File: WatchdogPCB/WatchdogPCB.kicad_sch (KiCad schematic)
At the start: 5 parts, among them J1 Conn_01x05_Socket, J2 Conn_01x05_Pin, J3 Screw_Terminal_01x03, J4 Power

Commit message: Working on the schematic
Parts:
- removed J1: Conn_01x05_Socket, Connector_Molex:Molex_KK-254_AE-6410-05A_1x05_P2.54mm_Vertical, symbol Connector:Conn_01x05_Socket
- removed J2: Conn_01x05_Pin, Connector_PinHeader_2.54mm:PinHeader_1x05_P2.54mm_Vertical, symbol Connector:Conn_01x05_Pin
- removed J3: Screw_Terminal_01x03, TerminalBlock:TerminalBlock_bornier-3_P5.08mm, symbol Connector:Screw_Terminal_01x03
- removed J4: Power, TerminalBlock:TerminalBlock_bornier-4_P5.08mm, symbol Connector:Screw_Terminal_01x04
- added J1: Screw_Terminal_01x03, symbol Connector:Screw_Terminal_01x03
- added J2: Screw_Terminal_01x04, symbol Connector:Screw_Terminal_01x04
- added J3: Screw_Terminal_01x02, symbol Connector:Screw_Terminal_01x02
- added J4: Conn_01x05_Pin, symbol Connector:Conn_01x05_Pin
- added JP1: Jumper_2_Open, symbol Jumper:Jumper_2_Open
- added JP2: Jumper_2_Bridged, symbol Jumper:Jumper_2_Bridged
- added R1, R2, R3, R4, R5, R6: R, symbol Device:R
- added RV1: R_Potentiometer, symbol Device:R_Potentiometer
- added TH1: Thermistor_NTC, symbol Device:Thermistor_NTC
- added U1: MCP602, symbol Amplifier_Operational:MCP602
- added U2: A1301EUA-T, symbol Sensor_Magnetic:A1301EUA-T
- added U3: DS3695N, DIP254P762X508-8, symbol DS3695N:DS3695N
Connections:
- net at A1.1 (D1/TX): now also U3.4 (DI)
- net at A1.10 (D7): now also U3.3 (DE)
- net at A1.19 (A0): now also R4.1
- net at A1.2 (D0/RX): now also U3.1 (RO)
- net at A1.20 (A1): now also R5.2, R6.1
- net +5V: now reaches A1.27 (+5V)
- net +5V: now also JP2.2 (B), RV1.1, U1.8 (V+), U3.8 (VCC)
- net GND: now reaches A1.29 (GND)
- net GND: now also A1.4 (GND), J2.4 (Pin_4), J3.2 (Pin_2), R3.2, R6.2, RV1.3, TH1.2, U1.4 (V-), U3.5 (GND)
- net at A1.30 (VIN): now also JP1.1 (A)
- net at A1.5 (D2): now also R2.2, U1.1
- net at A1.7 (D4): now also U3.2 (~{RE})
- new net: J3.1 (Pin_1), R3.1, R4.2, TH1.1
- new net: J4.1 (Pin_1), JP2.1 (A)
- new net: U1.5 (+), U1.6 (-)
- new net: R1.1, R2.1, U1.3 (+)
- new net: J1.2 (Pin_2), R1.2, U2.3 (VOUT)
- new net: RV1.2, U1.2 (-)
- new net: J1.3 (Pin_3), U2.1 (VCC)
- new net: J1.1 (Pin_1), U2.2 (GND)
- new net: J2.1 (Pin_1), U3.6 (DO/RI)
- new net: J2.2 (Pin_2), U3.7 (~{DO/}RI)
- new net +12V: J2.3 (Pin_3), JP1.2 (B), R5.1
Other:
- company: (none) -> Jotham Gates
- title: (none) -> Tractor Engine Watchdog

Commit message: Schematic finished
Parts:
- removed J1: Screw_Terminal_01x03, symbol Connector:Screw_Terminal_01x03
- removed J3: Screw_Terminal_01x02, symbol Connector:Screw_Terminal_01x02
- removed R3, R4: R, symbol Device:R
- added D1: D_Zener, symbol Device:D_Zener
- added D2: 1N5404, Diode_THT:D_DO-201AD_P15.24mm_Horizontal, symbol Diode:1N5404
- added F1: 3A, symbol Device:Fuse
- added J1: Oil pressure, symbol Connector:Screw_Terminal_01x01
- added J3: Hall effect speed, symbol Connector:Screw_Terminal_01x03
- added J5: Power, symbol Connector:Screw_Terminal_01x04
- added J6, J7: Thermistor 1, symbol Connector:Screw_Terminal_01x02
- added J8: Dashboard A, symbol Connector:Conn_01x03_Pin
- added J9: Dashboard B, symbol Connector:Conn_01x05_Pin
- added R1, R7, R8: 1k, symbol Device:R
- added R10, R9: 470, symbol Device:R
- added R2: 4.7k, symbol Device:R
- added TH2: Thermistor_NTC, symbol Device:Thermistor_NTC
- J2: value Screw_Terminal_01x04 -> Roll hoop
- J4: value Conn_01x05_Pin -> H bridge driver control
- JP1: renamed from JP2; value Jumper_2_Bridged -> 5V jumper
- JP2: renamed from JP1; value Jumper_2_Open -> 12V jumper
- R3: renamed from R1; value R -> 4.7k
- R4: renamed from R2; value R -> 120k
- R5: value R -> 100k
- R6: value R -> 39k
- RV1: value R_Potentiometer -> 10k
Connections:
- net +12V: now also D2.1 (K), J5.2 (Pin_2), R10.1, R9.1; no longer R5.1
- net +5V: now also U2.1 (VCC), J3.1 (Pin_1), J9.1 (Pin_1), J9.2 (Pin_2)
- net GND: now also U1.5 (+), U2.2 (GND), D1.2 (A), J3.3 (Pin_3), J5.3 (Pin_3), J5.4 (Pin_4), J6.2 (Pin_2), J7.2 (Pin_2), J8.2 (Pin_2), J8.3 (Pin_3), J9.5 (Pin_5), R1.2, TH2.2
- net at A1.19 (A0): now also R7.1
- net at TH1.1: now also J6.1 (Pin_1), R7.2, R9.2
- net at A1.11 (D8): now also D1.1 (K), R2.2
- net at A1.14 (D11): now also J4.5 (Pin_5)
- net at R5.2, R6.1: now also A1.21 (A2); no longer A1.20 (A1)
- net Button: now reaches A1.22 (A3)
- net Button: now also J8.1 (Pin_1)
- net SDA: now reaches A1.23 (A4)
- net SDA: now also J9.3 (Pin_3)
- net SCL: now reaches A1.24 (A5)
- net SCL: now also J9.4 (Pin_4)
- net at A1.6 (D3): now also J4.2 (Pin_2)
- net at A1.8 (D5): now also J4.3 (Pin_3)
- net at A1.9 (D6): now also J4.4 (Pin_4)
- net at U1.6 (-): now also U1.7; no longer U1.5 (+)
- net at R3.2, U2.3 (VOUT): now also J3.2 (Pin_2)
- net Threshold adjust: now reaches RV1.2, U1.2 (-)
- new net: J7.1 (Pin_1), R10.2, R8.2, TH2.1
- new net: A1.20 (A1), R8.1
- new net: J1.1 (Pin_1), R1.1, R2.1
- new net +BATT: D2.2 (A), F1.1, R5.1
- new net Power in: F1.2, J5.1 (Pin_1)
- no-connect marks 0 -> 10
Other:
- note added: "Battery voltage divider"
- note added: "Dashboard"
- note added: "H bridge control pins"
- note added: "Hall effect engine speed sensor"
- note added: "NTC Thermistors"
- note added: "Oil pressure switch"
- note added: "Power input and H bridge power"
- note added: "RS485 connection to roll hoop"
- note added: "Unused op amp"
- moved on the sheet: J2, J4, JP1, R3, R4, R5, R6, RV1, U1A, U1B, U2, U3

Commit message: Layout mostly done
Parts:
- removed J1: Oil pressure, symbol Connector:Screw_Terminal_01x01
- removed J3: Hall effect speed, symbol Connector:Screw_Terminal_01x03
- added H1, H2, H3, H4: MountingHole, MountingHole:MountingHole_3.2mm_M3_Pad, symbol Mechanical:MountingHole
- added J2: Speed & Oil, TerminalBlock:TerminalBlock_bornier-4_P5.08mm, symbol Connector:Screw_Terminal_01x04
- added R11, R12: 4.7k, Resistor_THT:R_Axial_DIN0207_L6.3mm_D2.5mm_P7.62mm_Horizontal, symbol Device:R
- D1: value D_Zener -> 5.1V; footprint (none) -> Diode_THT:D_A-405_P10.16mm_Horizontal
- F1: footprint (none) -> Fuse:Fuse_Blade_ATO_directSolder
- J1: renamed from J2; footprint (none) -> TerminalBlock:TerminalBlock_bornier-4_P5.08mm
- J3: renamed from J4; footprint (none) -> Connector_PinHeader_2.54mm:PinHeader_1x05_P2.54mm_Vertical
- J4: renamed from J5; footprint (none) -> TerminalBlock:TerminalBlock_bornier-4_P5.08mm
- J5: renamed from J6; footprint (none) -> TerminalBlock:TerminalBlock_bornier-2_P5.08mm
- J6: renamed from J7; value Thermistor 1 -> Thermistor 2; footprint (none) -> TerminalBlock:TerminalBlock_bornier-2_P5.08mm
- J7: renamed from J8; footprint (none) -> Connector_JST:JST_XH_B3B-XH-A_1x03_P2.50mm_Vertical
- J8: renamed from J9; footprint (none) -> Connector_JST:JST_XH_B5B-XH-A_1x05_P2.50mm_Vertical
- JP1, JP2: footprint (none) -> Connector_PinSocket_2.54mm:PinSocket_1x02_P2.54mm_Vertical
- R1: renamed from R3; footprint (none) -> Resistor_THT:R_Axial_DIN0207_L6.3mm_D2.5mm_P7.62mm_Horizontal
- R10, R5, R6, R7, R8, R9: footprint (none) -> Resistor_THT:R_Axial_DIN0207_L6.3mm_D2.5mm_P7.62mm_Horizontal
- R2: renamed from R1; footprint (none) -> Resistor_THT:R_Axial_DIN0207_L6.3mm_D2.5mm_P7.62mm_Horizontal
- R3: renamed from R4; footprint (none) -> Resistor_THT:R_Axial_DIN0207_L6.3mm_D2.5mm_P7.62mm_Horizontal
- R4: renamed from R2; footprint (none) -> Resistor_THT:R_Axial_DIN0207_L6.3mm_D2.5mm_P7.62mm_Horizontal
- RV1: footprint (none) -> Potentiometer_THT:Potentiometer_Piher_PT-10-V10_Vertical_Hole
- U2: renamed from U1; footprint (none) -> Package_DIP:DIP-8_W7.62mm_Socket_LongPads
- U3: footprint DIP254P762X508-8 -> Package_DIP:DIP-8_W7.62mm_Socket_LongPads
- renumbered U2 to U1
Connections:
- net +12V: no longer R10.1, R9.1
- net +5V: now also R10.1, R9.1, J2.1 (Pin_1), R11.1, R12.1
- net GND: now also J2.3 (Pin_3)
- net SCL: now also R12.2
- net SDA: now also R11.2
- net Hall effect: now reaches R1.2, U1.3 (VOUT)
- net Hall effect: now also J2.2 (Pin_2)
- net Oil: now reaches R2.1, R4.1
- net Oil: now also J2.4 (Pin_4)
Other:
- moved on the sheet: D1, R1, R2, R3, R4, RV1, U1, U2A, U2B

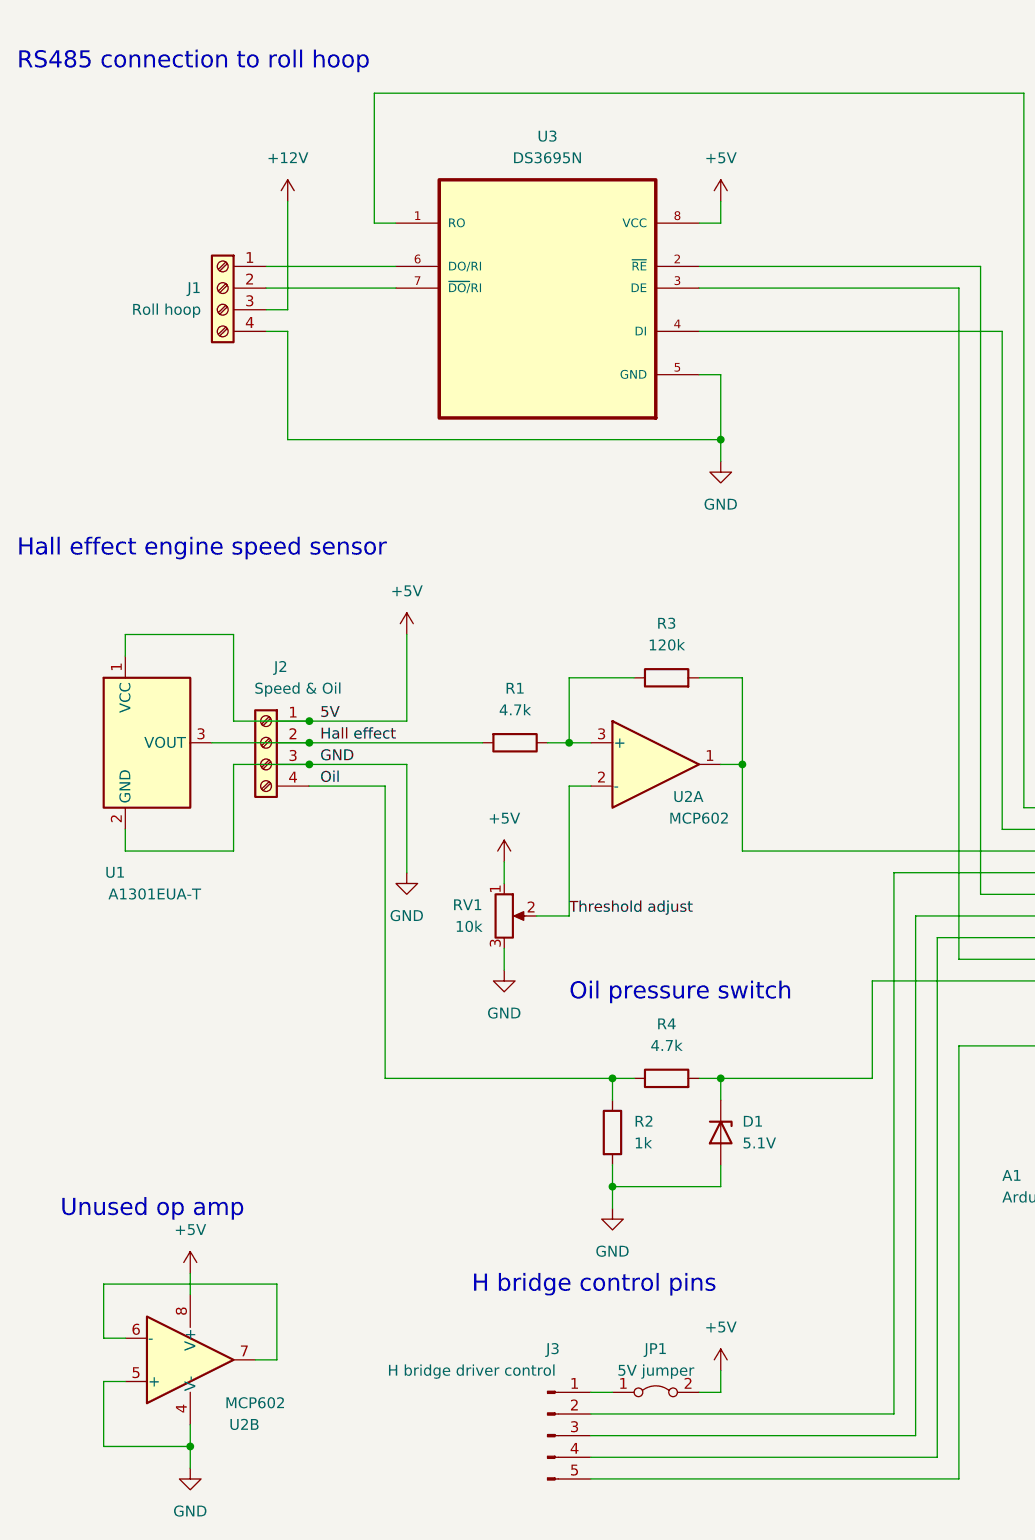
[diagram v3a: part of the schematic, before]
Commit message: Made fold go in two parts
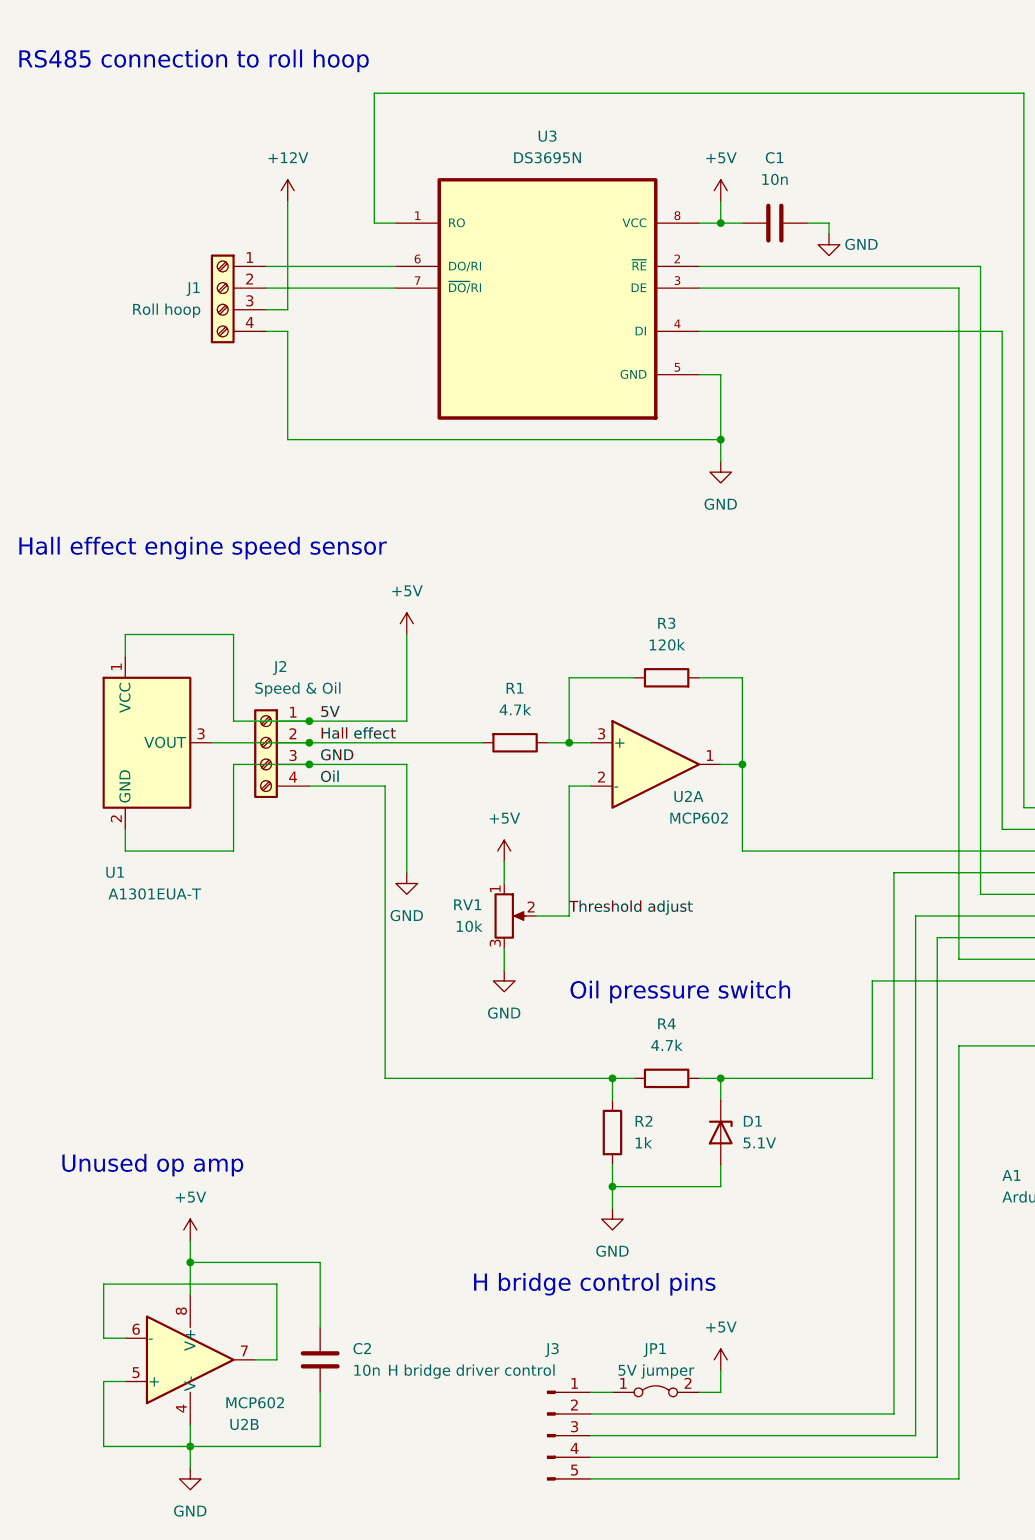
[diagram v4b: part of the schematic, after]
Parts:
- added C1, C2: 10n, Capacitor_THT:C_Rect_L7.0mm_W2.5mm_P5.00mm, symbol Device:C
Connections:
- net +5V: now also C1.1, C2.1
- net GND: now also C1.2, C2.2
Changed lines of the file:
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@@
   (junction (at 231.14 64.77) (diameter 0) (color 0 0 0 0)
   )
+  (junction (at 35.56 160.02) (diameter 0) (color 0 0 0 0)
+  )
   (junction (at 231.14 33.02) (diameter 0) (color 0 0 0 0)
   )
@@
   )
   (junction (at 223.52 151.13) (diameter 0) (color 0 0 0 0)
+  )
+  (junction (at 97.79 38.1) (diameter 0) (color 0 0 0 0)
   )
   (junction (at 144.78 30.48) (diameter 0) (color 0 0 0 0)
@@
     (stroke (width 0) (type default))
   )
+  (wire (pts (xy 50.8 167.64) (xy 50.8 160.02))
+    (stroke (width 0) (type default))
+  )
   (wire (pts (xy 45.72 171.45) (xy 43.18 171.45))
     (stroke (width 0) (type default))
@@
     (stroke (width 0) (type default))
   )
+  (wire (pts (xy 97.79 38.1) (xy 100.33 38.1))
+    (stroke (width 0) (type default))
+  )
   (wire (pts (xy 49.53 101.6) (xy 60.96 101.6))
     (stroke (width 0) (type default))
@@
     (stroke (width 0) (type default))
   )
-  (wire (pts (xy 35.56 161.29) (xy 35.56 163.83))
+  (wire (pts (xy 35.56 157.48) (xy 35.56 160.02))
     (stroke (width 0) (type default))
   )
@@
     (stroke (width 0) (type default))
   )
+  (wire (pts (xy 110.49 38.1) (xy 107.95 38.1))
+    (stroke (width 0) (type default))
+  )
   (wire (pts (xy 40.64 86.36) (xy 40.64 96.52))
     (stroke (width 0) (type default))
@@
     (stroke (width 0) (type default))
   )
+  (wire (pts (xy 35.56 160.02) (xy 35.56 163.83))
+    (stroke (width 0) (type default))
+  )
   (wire (pts (xy 118.11 114.3) (xy 135.89 114.3))
     (stroke (width 0) (type default))
@@
     (stroke (width 0) (type default))
   )
+  (wire (pts (xy 110.49 39.37) (xy 110.49 38.1))
+    (stroke (width 0) (type default))
+  )
   (wire (pts (xy 115.57 138.43) (xy 97.79 138.43))
     (stroke (width 0) (type default))
@@
     (stroke (width 0) (type default))
   )
+  (wire (pts (xy 50.8 175.26) (xy 50.8 181.61))
+    (stroke (width 0) (type default))
+  )
   (wire (pts (xy 245.11 146.05) (xy 256.54 146.05))
     (stroke (width 0) (type default))
@@
     (stroke (width 0) (type default))
   )
+  (wire (pts (xy 50.8 160.02) (xy 35.56 160.02))
+    (stroke (width 0) (type default))
+  )
   (wire (pts (xy 161.29 129.54) (xy 242.57 129.54))
     (stroke (width 0) (type default))
@@
   )
   (wire (pts (xy 44.45 48.26) (xy 46.99 48.26))
+    (stroke (width 0) (type default))
+  )
+  (wire (pts (xy 50.8 181.61) (xy 35.56 181.61))
     (stroke (width 0) (type default))
   )
@@
     (effects (font (size 2 2)) (justify right bottom))
   )
-  (text "Unused op amp" (at 20.32 154.94 0)
+  (text "Unused op amp" (at 20.32 149.86 0)
     (effects (font (size 2 2)) (justify left bottom))
   )
@@
         (path "/01720b08-9f76-4170-adb2-58115ea6550d"
           (reference "H2") (unit 1)
+        )
+      )
+    )
+  )
+  (symbol (lib_id "Device:C") (at 104.14 38.1 90) (unit 1)
+    (in_bom yes) (on_board yes) (dnp no) (fields_autoplaced)
+    (property "Reference" "C1" (at 104.14 30.48 90)
+      (effects (font (size 1.27 1.27)))
+    )
+    (property "Value" "10n" (at 104.14 33.02 90)
+      (effects (font (size 1.27 1.27)))
+    )
+    (property "Footprint" "Capacitor_THT:C_Rect_L7.0mm_W2.5mm_P5.00mm" (at 107.95 37.1348 0)
+      (effects (font (size 1.27 1.27)) hide)
+    )
+    (property "Datasheet" "~" (at 104.14 38.1 0)
+      (effects (font (size 1.27 1.27)) hide)
+    )
+    (pin "1")
+    (pin "2")
+    (instances
+      (project "WatchdogPCB"
+        (path "/01720b08-9f76-4170-adb2-58115ea6550d"
+          (reference "C1") (unit 1)
         )
       )
@@
     )
   )
+  (symbol (lib_id "Device:C") (at 50.8 171.45 0) (unit 1)
+    (in_bom yes) (on_board yes) (dnp no) (fields_autoplaced)
+    (property "Reference" "C2" (at 54.61 170.18 0)
+      (effects (font (size 1.27 1.27)) (justify left))
+    )
+    (property "Value" "10n" (at 54.61 172.72 0)
+      (effects (font (size 1.27 1.27)) (justify left))
+    )
+    (property "Footprint" "Capacitor_THT:C_Rect_L7.0mm_W2.5mm_P5.00mm" (at 51.7652 175.26 0)
+      (effects (font (size 1.27 1.27)) hide)
+    )
+    (property "Datasheet" "~" (at 50.8 171.45 0)
+      (effects (font (size 1.27 1.27)) hide)
+    )
+    (pin "1")
+    (pin "2")
+    (instances
+      (project "WatchdogPCB"
+        (path "/01720b08-9f76-4170-adb2-58115ea6550d"
+          (reference "C2") (unit 1)
+        )
+      )
+    )
+  )
   (symbol (lib_id "power:+5V") (at 231.14 20.32 0) (unit 1)
     (in_bom yes) (on_board yes) (dnp no) (fields_autoplaced)
@@
     )
   )
+  (symbol (lib_id "power:GND") (at 110.49 39.37 0) (unit 1)
+    (in_bom yes) (on_board yes) (dnp no)
+    (property "Reference" "#PWR027" (at 110.49 45.72 0)
+      (effects (font (size 1.27 1.27)) hide)
+    )
+    (property "Value" "GND" (at 114.3 40.64 0)
+      (effects (font (size 1.27 1.27)))
+    )
+    (property "Footprint" "" (at 110.49 39.37 0)
+      (effects (font (size 1.27 1.27)) hide)
+    )
+    (property "Datasheet" "" (at 110.49 39.37 0)
+      (effects (font (size 1.27 1.27)) hide)
+    )
+    (pin "1")
+    (instances
+      (project "WatchdogPCB"
+        (path "/01720b08-9f76-4170-adb2-58115ea6550d"
+          (reference "#PWR027") (unit 1)
+        )
+      )
+    )
+  )
   (symbol (lib_id "Connector:Conn_01x05_Pin") (at 77.47 180.34 0) (unit 1)
     (in_bom yes) (on_board yes) (dnp no)
@@
     )
   )
-  (symbol (lib_id "power:+5V") (at 35.56 161.29 0) (unit 1)
-    (in_bom yes) (on_board yes) (dnp no) (fields_autoplaced)
-    (property "Reference" "#PWR01" (at 35.56 165.1 0)
-      (effects (font (size 1.27 1.27)) hide)
-    )
-    (property "Value" "+5V" (at 35.56 156.21 0)
-      (effects (font (size 1.27 1.27)))
-    )
-    (property "Footprint" "" (at 35.56 161.29 0)
-      (effects (font (size 1.27 1.27)) hide)
-    )
-    (property "Datasheet" "" (at 35.56 161.29 0)
-      (effects (font (size 1.27 1.27)) hide)
-    )
+  (symbol (lib_id "power:+5V") (at 35.56 157.48 0) (unit 1)
+    (in_bom yes) (on_board yes) (dnp no)
+    (property "Reference" "#PWR01" (at 35.56 161.29 0)
+      (effects (font (size 1.27 1.27)) hide)
+    )
+    (property "Value" "+5V" (at 35.56 152.4 0)
+      (effects (font (size 1.27 1.27)))
+    )
+    (property "Footprint" "" (at 35.56 157.48 0)
+      (effects (font (size 1.27 1.27)) hide)
+    )
+    (property "Datasheet" "" (at 35.56 157.48 0)
+      (effects (font (size 1.27 1.27)) hide)
+    )
